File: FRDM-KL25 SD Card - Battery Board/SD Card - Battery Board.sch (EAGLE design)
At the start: 64 parts, among them J3 SSW-108-02-S-D, J4 SSW-110-02-S-D, J5 SSW-108-02-S-D, J6 SSW-106-02-S-D, U1 TPS63001, U2 TPS63002, U3 BQ27510DRZT-G3, U4 BQ24210DQCT

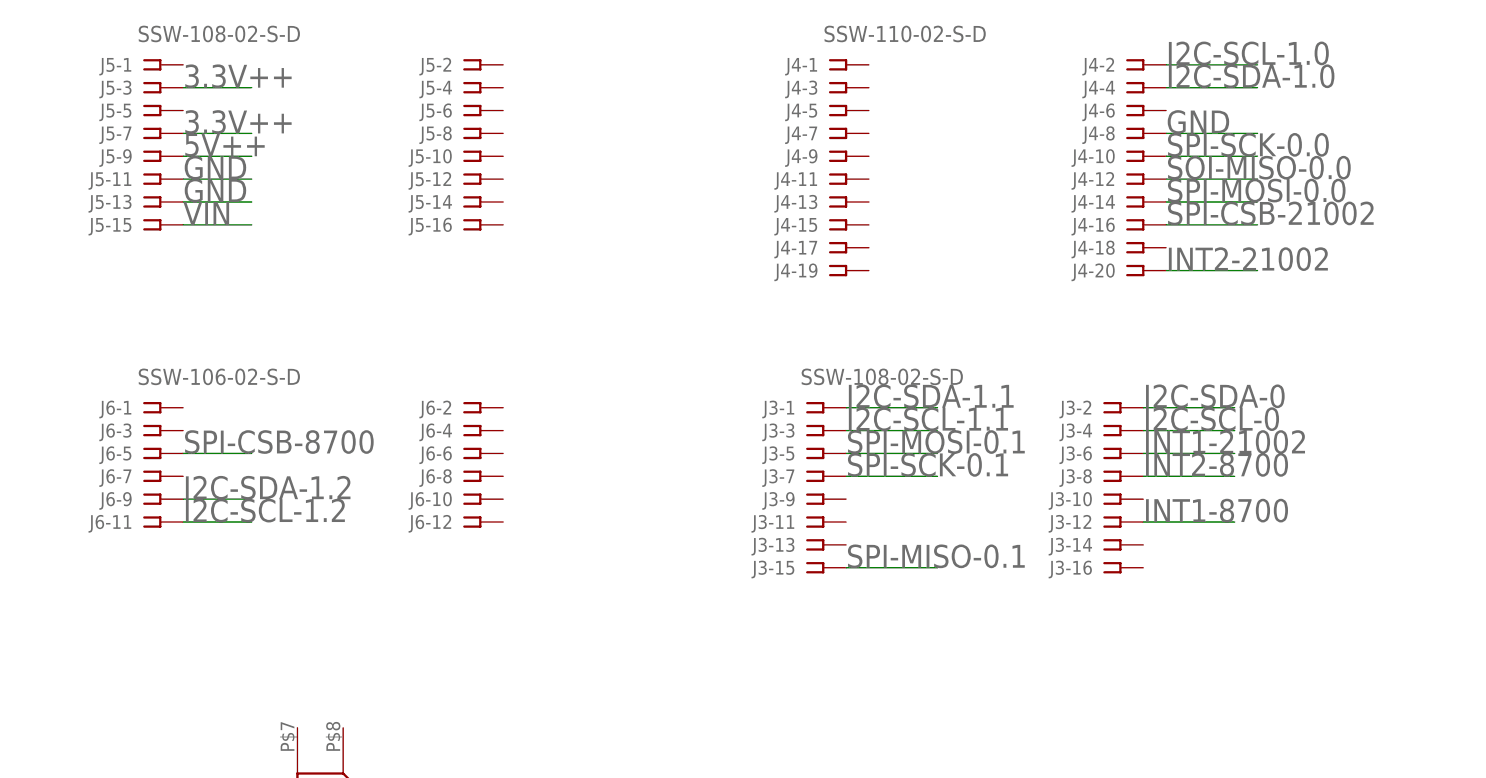
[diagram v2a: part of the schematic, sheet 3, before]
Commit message: FRDM-KL25Z: Corrected J3, J4, J5 and J6 connections on the schematic. Jumpers where added for 3V3, 5V and TPS63001 EN and BQ24210 EN. SPI Connections have been labled to enable SD card to connect to PD1, PD2 and PD3. Layed out and connected TPS63002 circuit as well as BQ42410 circuit.
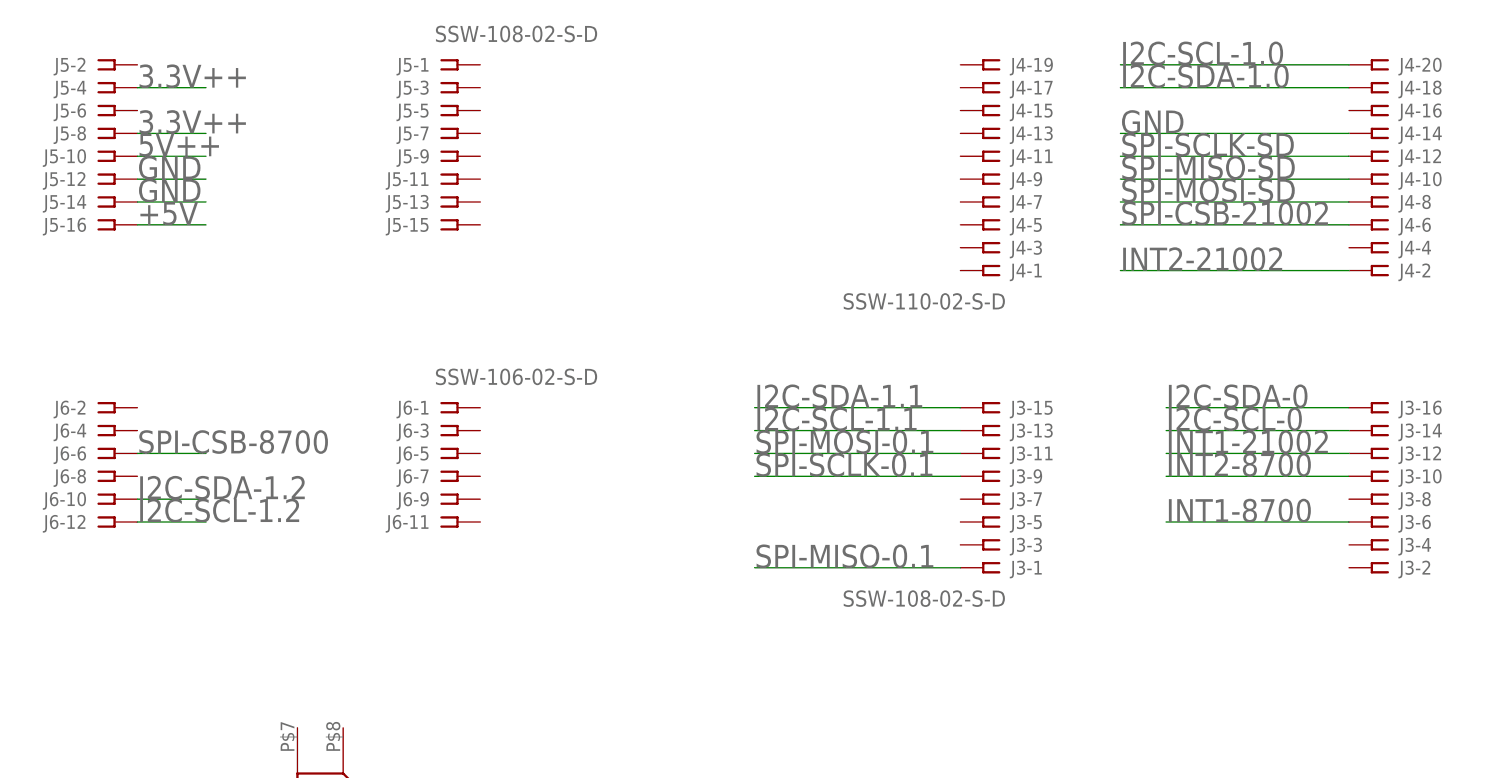
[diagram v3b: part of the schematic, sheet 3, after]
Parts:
- added J10, J9: SSW-103-02-S-S, Kas-Connectors:SSW-103-02-S-S
- added J7, J8: SSW-102-02-S-S, Kas-Connectors:SSW-102-02-S-S
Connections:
- removed net 3.3V_KL25Z--ADD-JUMPER: D3.C
- removed net 5V_KL25Z--ADD-JUMPER: D4.C
- removed net SOI-MISO-0.0: J4-12.1
- removed net SPI-MISO: J1.DAT0, R5.1
- removed net SPI-MOSI: J1.CMD, R3.1
- removed net SPI-MOSI-0.0: J4-14.1
- removed net SPI-SCK-0.0: J4-10.1
- removed net SPI-SCK-0.1: J3-7.1
- removed net SPI-SCLK: J1.CLK, R4.1
- removed net VIN: J5-15.1
- new net 3.3V_KL25Z: D3.C, J7-2.1
- new net 3V3+: J7-1.1
- new net 5V_KL25Z: D4.C, J8-2.1
- new net N$2: J10-2.1, U1.EN
- new net SELF_EN: J9-1.1, R25.1
- new net SPI-MISO-SD: J1.DAT0, J4-10.1, R5.1
- new net SPI-MOSI-SD: J1.CMD, J4-8.1, R3.1
- new net SPI-SCLK-0.1: J3-9.1
- new net SPI-SCLK-SD: J1.CLK, J4-12.1, R4.1
- new net UC_3V3_EN: J10-1.1
- new net UC_EN_CHARGE: J9-3.1
- new net VCC: C4.2, D4.A, U2.FB, U2.VOUT
- net !BAT_LOW: now also J10-3.1; no longer U1.EN
- net !FN: now also J9-2.1; no longer R25.1
- net +5V: now also J5-16.1, J8-1.1; no longer C4.2, D4.A, U2.FB, U2.VOUT
- net 3.3V++: now also J5-4.1, J5-8.1; no longer J5-3.1, J5-7.1
- net 5V++: now also J5-10.1; no longer J5-9.1
- net GND: now also J4-14.1, J5-12.1, J5-14.1; no longer J4-8.1, J5-11.1, J5-13.1
- net I2C-SCL-0: now also J3-14.1; no longer J3-4.1
- net I2C-SCL-1.0: now also J4-20.1; no longer J4-2.1
- net I2C-SCL-1.1: now also J3-13.1; no longer J3-3.1
- net I2C-SCL-1.2: now also J6-12.1; no longer J6-11.1
- net I2C-SDA-0: now also J3-16.1; no longer J3-2.1
- net I2C-SDA-1.0: now also J4-18.1; no longer J4-4.1
- net I2C-SDA-1.1: now also J3-15.1; no longer J3-1.1
- net I2C-SDA-1.2: now also J6-10.1; no longer J6-9.1
- net INT1-21002: now also J3-12.1; no longer J3-6.1
- net INT1-8700: now also J3-6.1; no longer J3-12.1
- net INT2-21002: now also J4-2.1; no longer J4-20.1
- net INT2-8700: now also J3-10.1; no longer J3-8.1
- net SPI-CSB-21002: now also J4-6.1; no longer J4-16.1
- net SPI-CSB-8700: now also J6-6.1; no longer J6-5.1
- net SPI-MISO-0.1: now also J3-1.1; no longer J3-15.1
- net SPI-MOSI-0.1: now also J3-11.1; no longer J3-5.1
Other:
- moved on the sheet: J3-1, J3-10, J3-11, J3-12, J3-13, J3-14, J3-15, J3-16, J3-2, J3-3, J3-4, J3-5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

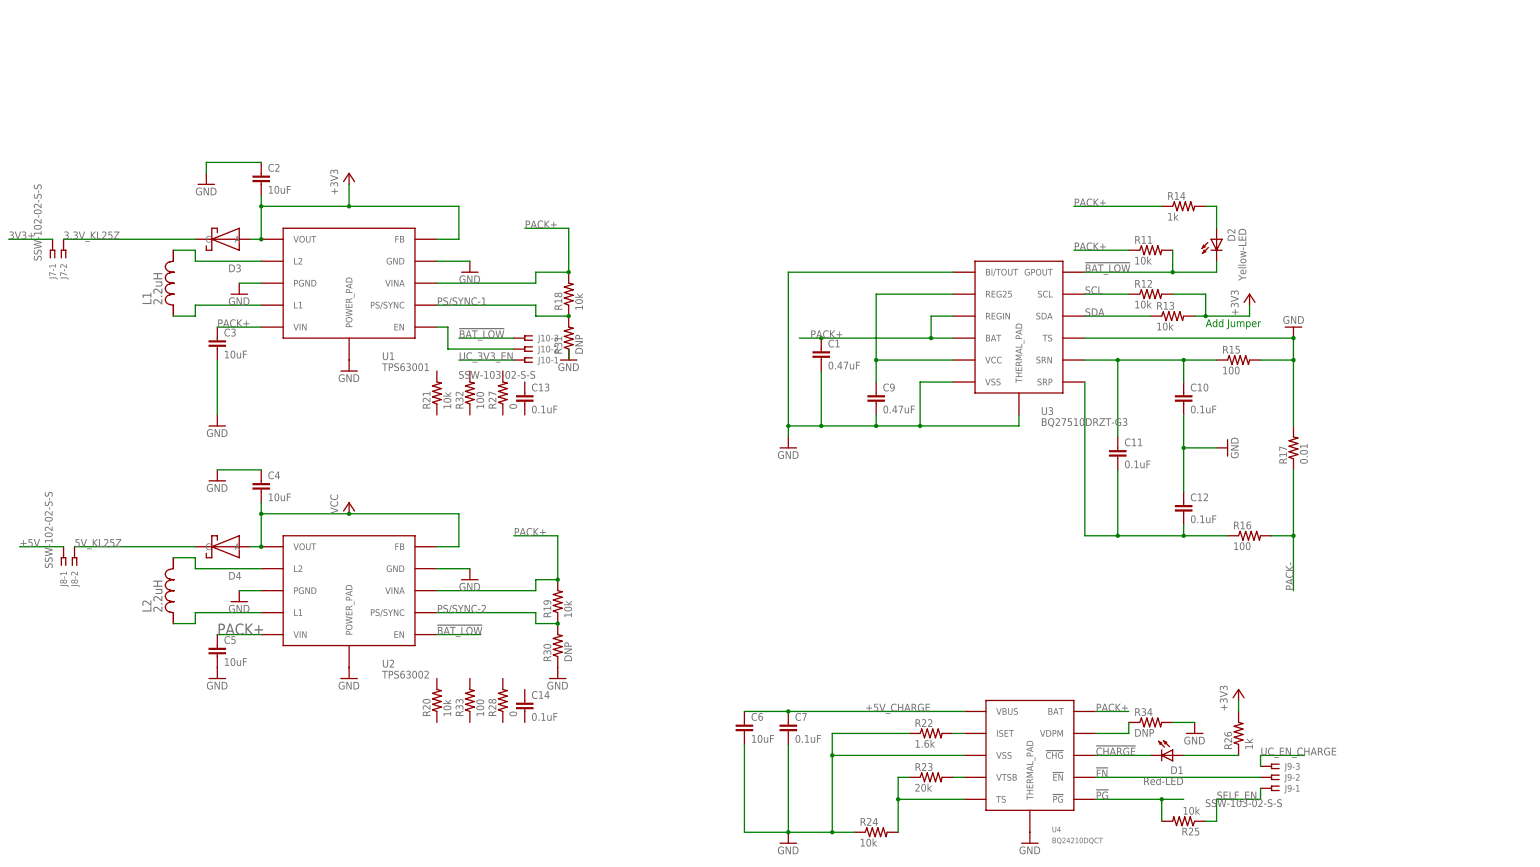
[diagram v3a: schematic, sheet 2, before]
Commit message: FRDM-KL25Z: Connected all major ICs to their respective components ad moved them into a resanable location. I2C connections were made as were the 3V3 and 5V connctions to the main board. It was decided to leave VIN unconnected as this in reality will not be needed as a 3V3 rail is avaiable from the battery. Headers were added to allow for connecting and disconnecting the 3V3 and 5V rails as well as selecting how to enable/disable the buck/boost ICs. Headers were also added to allow the choosing of I2C-0 or I2C-1. Also added was the ability to pull the I2C to 3V3 or if provided by another board in the stack to do so there instead.
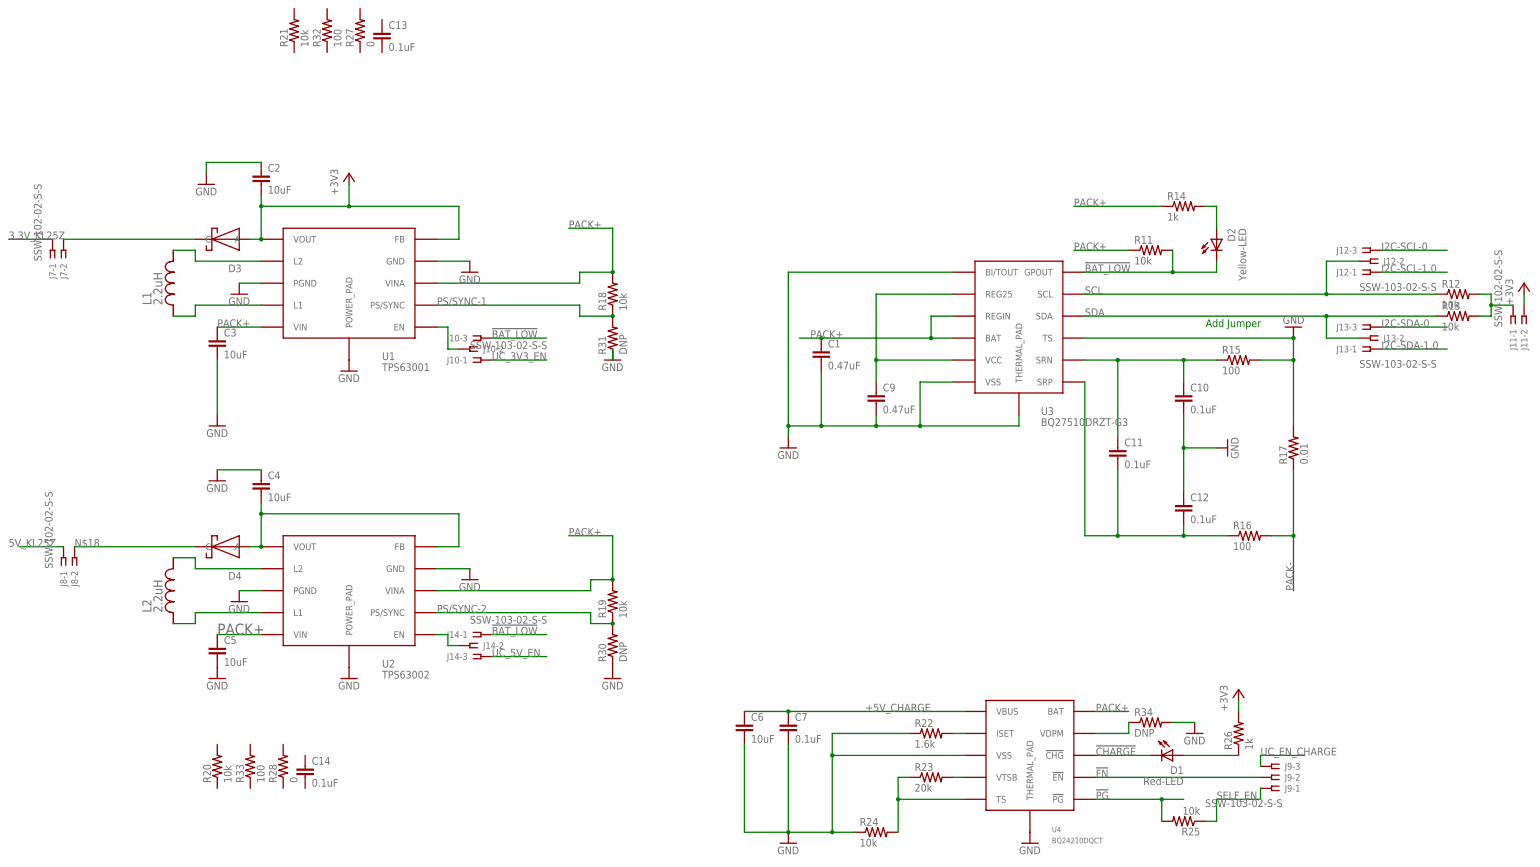
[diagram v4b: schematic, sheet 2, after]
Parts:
- added J11: SSW-102-02-S-S, Kas-Connectors:SSW-102-02-S-S
- added J12, J13, J14: SSW-103-02-S-S, Kas-Connectors:SSW-103-02-S-S
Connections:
- net VCC renamed N$20
- removed net +5V: J5-16.1, J8-1.1
- removed net 3.3V++: J5-4.1, J5-8.1
- removed net 3V3+: J7-1.1
- removed net 5V++: J5-10.1
- new net N$13: J14-2.1, U2.EN
- new net N$17: D3.C, J7-2.1
- new net N$18: D4.C, J8-2.1
- new net N$4: J11-1.1, R12.2, R13.2
- new net UC_5V_EN: J14-3.1
- new net VIN: J5-16.1
- net !BAT_LOW: now also J14-1.1; no longer U2.EN
- net +3V3: now also J11-2.1; no longer R12.2, R13.2
- net 3.3V_KL25Z: now also J5-4.1, J5-8.1, J7-1.1; no longer D3.C, J7-2.1
- net 5V_KL25Z: now also J5-10.1, J8-1.1; no longer D4.C, J8-2.1
- net I2C-SCL-0: now also J12-3.1
- net I2C-SCL-1.0: now also J12-1.1
- net I2C-SDA-0: now also J13-3.1
- net I2C-SDA-1.0: now also J13-1.1
- net SCL: now also J12-2.1
- net SDA: now also J13-2.1
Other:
- moved on the sheet: C13, C14, J10-1, J10-2, J10-3, R12, R13, R18, R19, R20, R21, R27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

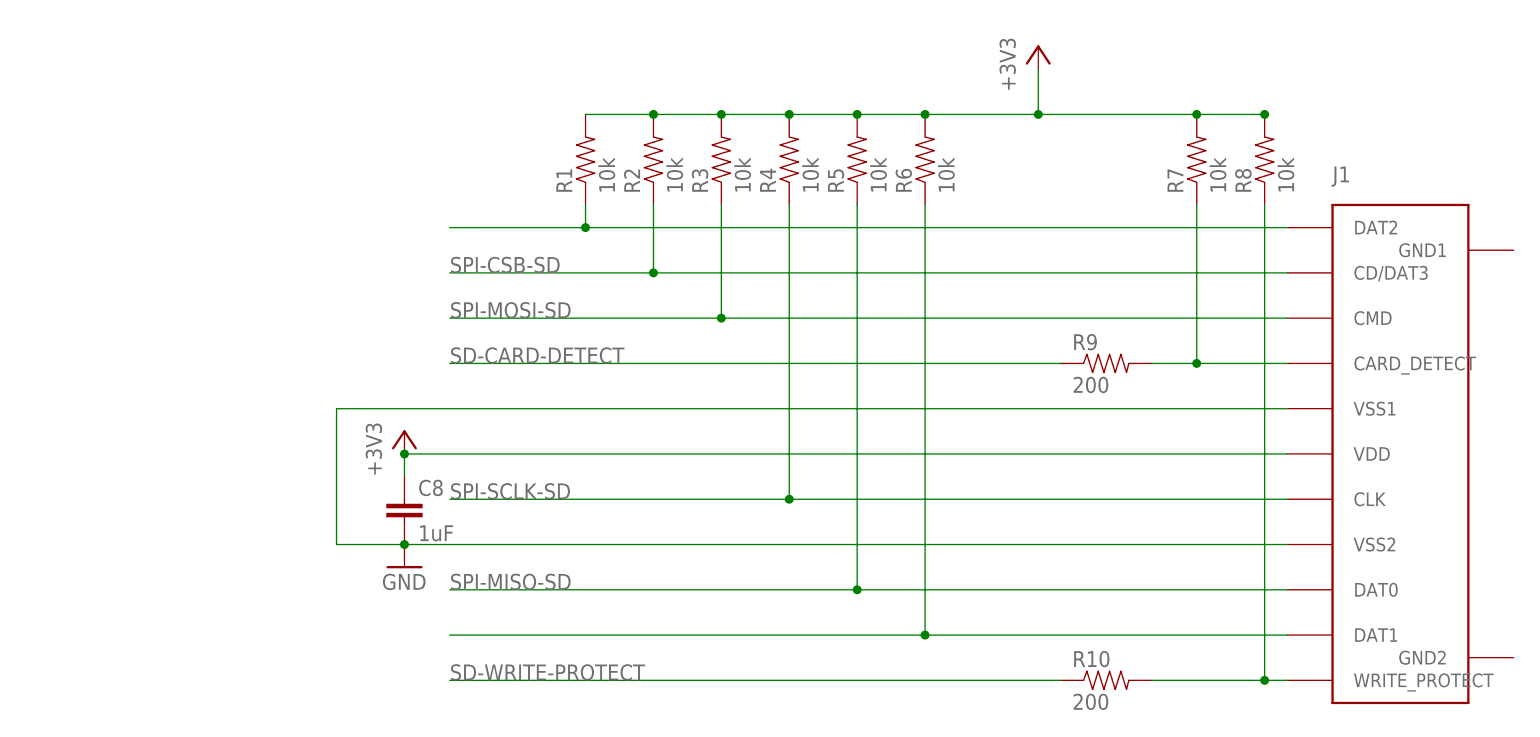
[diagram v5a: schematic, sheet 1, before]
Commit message: FRDM-KL25Z-I: Cleaned up a few routed connections and routed most of the battery connections. The remaining connections are the LEDs and the SD card. There are a few connections that have not yet been made these are: SD-CS, UC-3V3-EN, UC-5V-EN and UC-EN-CHARGE, tickets will be created for these to ensure they are completed before the board is sentout
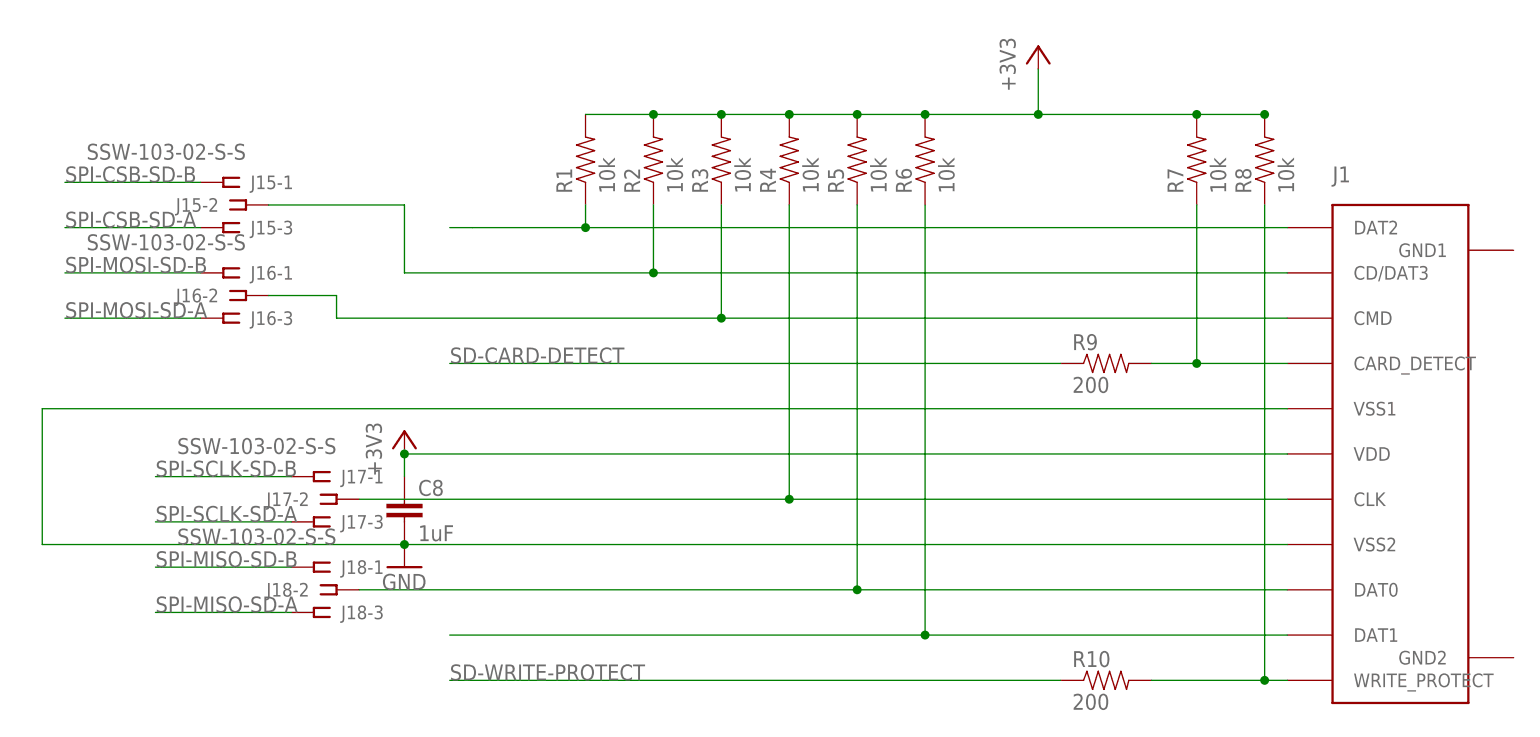
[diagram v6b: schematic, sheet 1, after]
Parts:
- added J15, J16, J17, J18: SSW-103-02-S-S, Kas-Connectors:SSW-103-02-S-S
- added J19: 501568-0207-V2, Kas-Connectors:501568-0207-V2
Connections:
- net I2C-SCL-1.0 renamed I2C-SCL-1
- net I2C-SDA-1.0 renamed I2C-SDA-1
- removed net SPI-CSB-SD: J1.CD/DAT3, R2.1
- removed net SPI-MISO-0.1: J3-1.1
- removed net SPI-MISO-SD: J1.DAT0, J4-10.1, R5.1
- removed net SPI-MOSI-0.1: J3-11.1
- removed net SPI-MOSI-SD: J1.CMD, J4-8.1, R3.1
- removed net SPI-SCLK-0.1: J3-9.1
- removed net SPI-SCLK-SD: J1.CLK, J4-12.1, R4.1
- new net N$23: J1.CD/DAT3, J15-2.1, R2.1
- new net N$27: J1.CMD, J16-2.1, R3.1
- new net N$30: J1.CLK, J17-2.1, R4.1
- new net N$35: J1.DAT0, J18-2.1, R5.1
- new net SPI-CSB-SD-A: J15-3.1
- new net SPI-CSB-SD-B: J15-1.1
- new net SPI-MISO-SD-A: J18-3.1, J4-10.1
- new net SPI-MISO-SD-B: J18-1.1, J3-1.1
- new net SPI-MOSI-SD-A: J16-3.1, J4-8.1
- new net SPI-MOSI-SD-B: J16-1.1, J3-11.1
- new net SPI-SCLK-SD-A: J17-3.1, J4-12.1
- new net SPI-SCLK-SD-B: J17-1.1, J3-9.1
- net PACK+: now also J19G$1.1
- net PACK-: now also J19G$2.1
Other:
- note removed: "NEED TO ADD BATTERY CONNECTION"
